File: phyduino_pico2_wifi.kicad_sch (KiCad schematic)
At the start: 12 parts, among them U11 ESP32-C6-MINI-1-H4

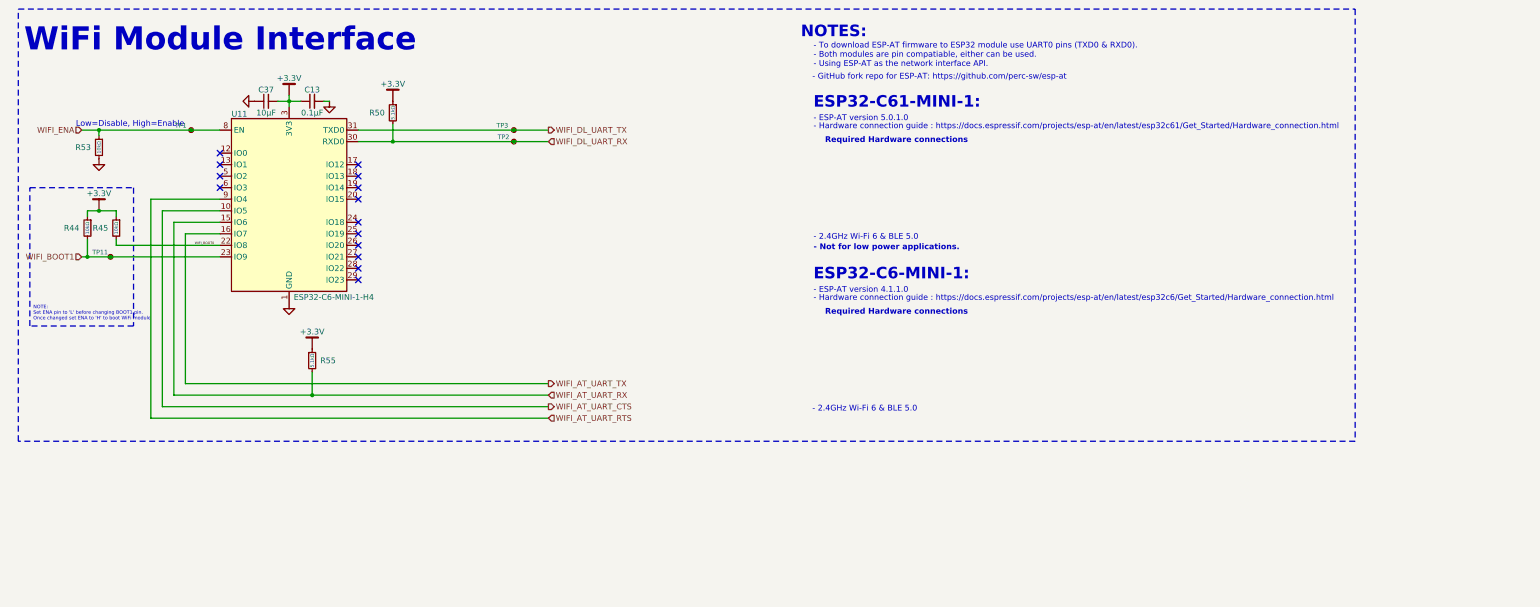
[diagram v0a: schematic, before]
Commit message: Resized schematic sheet to A from B. Add micropython logo to back silkscreen. Regenerated gerber files
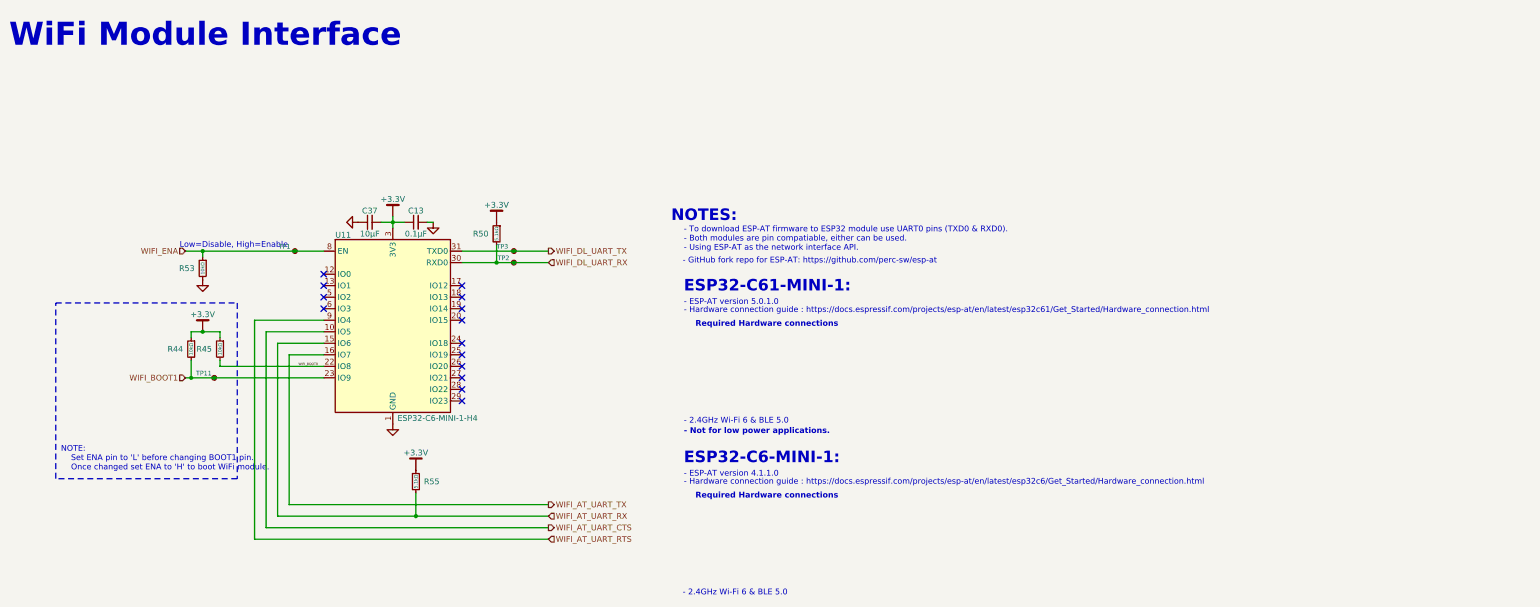
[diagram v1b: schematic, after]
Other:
- moved on the sheet: C13, C37, R44, R45, R50, R53, R55, TP1, TP11, TP2, TP3, U11

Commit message: Updated part numbers and distributor part nummbers after BoM review.
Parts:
- C13: DIGIKEY PN 490-14514-1-ND -> (none); DIGIKEY_PN (none) -> 490-14514-1-ND; DIGKEY MANUFACTURER Murata Electronics -> (none); KiLib_Generator SMD_2terminal_chip_molded -> (none); LCSC MANUFACTURER CCTC -> (none); LCSC PN C5142567 -> (none); LCSC_PN (none) -> C85858; MOUSER_PN (none) -> 81-GCM155R71H104KE2J; PN TCC0402X7R104M500AT -> GCM155R71H104KE02J; Tolerance (none) -> ±10%
- C37: DIGIKEY PN 490-10748-1-ND -> (none); DIGIKEY_PN (none) -> 587-4893-1-ND; DIGKEY MANUFACTURER Murata Electronics -> (none); KiLib_Generator SMD_2terminal_chip_molded -> (none); LCSC MANUFACTURER AIDE CAPACITOR -> (none); LCSC PN C49326680 -> (none); LCSC_PN (none) -> C440198; MOUSER_PN (none) -> 603-CC0805KKX59BB106; PN 0805X5R106K350NT -> GMK212BBJ106KG-T; Tolerance (none) -> ±10%
- R44, R45, R53: DIGIKEY PN 13-RC0402FR-131K1LCT-ND -> (none); DIGIKEY_PN (none) -> 311-10.0KLRCT-ND; DIGKEY MANUFACTURER YAGEO -> (none); KiLib_Generator SMD_2terminal_chip_molded -> (none); LCSC MANUFACTURER FOJAN -> (none); LCSC PN C2909306 -> (none); LCSC_PN (none) -> C60490; MOUSER_PN (none) -> 603-RC0402FR-0710KL; PN FRC0402F1101TS -> RC0402FR-0710KL
- R50, R55: DIGIKEY_PN (none) -> 311-5.10KLRCT-ND; KiLib_Generator SMD_2terminal_chip_molded -> (none); LCSC_PN (none) -> C105872; MOUSER_PN (none) -> 603-RC0402FR-075K1L; PN (none) -> RC0402FR-075K1L
- U11: DIGIKEY_PN (none) -> 1965-ESP32-C6-MINI-1-H4CT-ND; MOUSER_PN (none) -> 356-ESP32C6MINI1-H4; PN (none) -> ${VALUE}
